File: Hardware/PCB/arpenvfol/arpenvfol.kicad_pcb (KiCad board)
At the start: 2 copper layers, 0 parts

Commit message: Better .gitignore; misc revisions
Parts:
- added C1: 10uF, ao_tht:CP_Radial_D6.3mm_P2.50mm, B.Cu at (96.2, 83.5)
- added C11: 20pF, ao_tht:C_Disc_D3.0mm_W1.6mm_P2.50mm, B.Cu at (83.5, 63.2)
- added C12: 1uF, ao_tht:C_Rect_L7.2mm_W2.5mm_P5.00mm_FKS2_FKP2_MKS2_MKP2, B.Cu at (91.1, 40.3)
- added C13: 100nF, ao_tht:C_Rect_L7.2mm_W2.5mm_P5.00mm_FKS2_FKP2_MKS2_MKP2, B.Cu at (98.7, 50.4)
- added C14: 10uF, ao_tht:C_Radial_D8.0mm_H11.5mm_P3.50mm, B.Cu at (116.5, 108.9)
- added C15: 10nF, ao_tht:C_Rect_L7.2mm_W2.5mm_P5.00mm_FKS2_FKP2_MKS2_MKP2, B.Cu at (106.3, 40.3)
- added C16: 10pF, ao_tht:C_Disc_D3.0mm_W1.6mm_P2.50mm, B.Cu at (108.9, 67.0)
- added C17: 2nF, ao_tht:C_Rect_L7.2mm_W2.5mm_P5.00mm_FKS2_FKP2_MKS2_MKP2, B.Cu at (114.0, 50.4)
- added C18: 47pF, ao_tht:C_Disc_D3.0mm_W1.6mm_P2.50mm, B.Cu at (119.0, 67.0)
- added C19: 1nF, ao_tht:C_Rect_L7.2mm_W2.5mm_P5.00mm_FKS2_FKP2_MKS2_MKP2, B.Cu at (115.3, 61.9)
- added C2: 10uF, ao_tht:CP_Radial_D6.3mm_P2.50mm, B.Cu at (103.8, 83.5)
- added C20: 100nF, ao_tht:C_Disc_D3.0mm_W1.6mm_P2.50mm, B.Cu at (91.1, 63.2)
- added C21: 100nF, ao_tht:C_Disc_D3.0mm_W1.6mm_P2.50mm, B.Cu at (111.4, 61.9)
- added C3: 10uF, ao_tht:C_Radial_D8.0mm_H11.5mm_P3.50mm, B.Cu at (79.7, 108.9)
- added C4: 100uF, ao_tht:CP_Radial_D6.3mm_P2.50mm, B.Cu at (87.3, 116.5)
- added C5: 100nF, ao_tht:C_Rect_L7.2mm_W2.5mm_P5.00mm_FKS2_FKP2_MKS2_MKP2, B.Cu at (106.3, 136.8)
- added C6: 20pF, ao_tht:C_Disc_D3.0mm_W1.6mm_P2.50mm, B.Cu at (88.6, 70.8)
- added C7: 20pF, ao_tht:C_Disc_D3.0mm_W1.6mm_P2.50mm, B.Cu at (81.0, 83.5)
- added C8: 220uF, ao_tht:CP_Radial_D6.3mm_P2.50mm, B.Cu at (87.3, 124.1)
- added C9: 220uF, ao_tht:CP_Radial_D6.3mm_P2.50mm, B.Cu at (91.1, 98.7)
- added D1: 1N5817, ao_tht:D_DO-41_SOD81_P10.16mm_Horizontal, B.Cu at (94.9, 78.4)
- added D2: 1N5817, ao_tht:D_DO-41_SOD81_P10.16mm_Horizontal, B.Cu at (110.2, 94.9)
- added D3: 1N4148, ao_tht:D_DO-35_SOD27_P7.62mm_Horizontal, B.Cu at (96.2, 74.6)
- added D4: 1N4148, ao_tht:D_DO-35_SOD27_P7.62mm_Horizontal, B.Cu at (83.5, 83.5)
- added GRAF1: Holes, arpenvfol:arpenvfol_panel_holes, F.Cu at (100.0, 100.0)
- added J1: Synth_power_2x5, ao_tht:Power_Header, B.Cu at (116.5, 94.9)
- added J10: 3_pin_Molex_header, ao_tht:Molex_KK-254_AE-6410-03A_1x03_P2.54mm_Vertical, B.Cu at (97.5, 135.6)
- added J2: AudioJack2_SwitchT, ao_tht:Jack_6.35mm_PJ_629HAN_slots, F.Cu at (87.5, 150.0)
- added J3: AudioJack2_SwitchT, ao_tht:Jack_6.35mm_PJ_629HAN_slots, F.Cu at (112.5, 125.0)
- added J4: AudioJack2_SwitchT, ao_tht:Jack_6.35mm_PJ_629HAN_slots, F.Cu at (112.5, 150.0)
- added J5: AudioJack2, ao_tht:Jack_6.35mm_PJ_629HAN_slots, F.Cu at (112.5, 175.0)
- added J6: AudioJack2, ao_tht:Jack_6.35mm_PJ_629HAN_slots, F.Cu at (87.5, 175.0)
- added J8: 2_pin_Molex_header, ao_tht:Molex_KK-254_AE-6410-02A_1x02_P2.54mm_Vertical, B.Cu at (84.8, 135.6)
- added Q1: 2N3904, ao_tht:TO-92_Inline_Wide, B.Cu at (88.6, 111.4)
- added Q2: 2N3904, ao_tht:TO-92_Inline_Wide, B.Cu at (94.9, 111.4)
- added R1: 1k, ao_tht:R_Axial_DIN0207_L6.3mm_D2.5mm_P10.16mm_Horizontal, B.Cu at (79.7, 91.1)
- added R10: 1k, ao_tht:R_Axial_DIN0207_L6.3mm_D2.5mm_P10.16mm_Horizontal, B.Cu at (96.2, 91.1)
- added R11: 1k, ao_tht:R_Axial_DIN0207_L6.3mm_D2.5mm_P10.16mm_Horizontal, B.Cu at (100.0, 116.5)
- added R12: 100k, ao_tht:R_Axial_DIN0207_L6.3mm_D2.5mm_P10.16mm_Horizontal, B.Cu at (83.5, 40.3)
- added R13: 120k, ao_tht:R_Axial_DIN0207_L6.3mm_D2.5mm_P10.16mm_Horizontal, B.Cu at (91.1, 59.4)
- added R14: 100k, ao_tht:R_Axial_DIN0207_L6.3mm_D2.5mm_P10.16mm_Horizontal, B.Cu at (81.0, 55.5)
- added R15: 2.7k, ao_tht:R_Axial_DIN0207_L6.3mm_D2.5mm_P10.16mm_Horizontal, B.Cu at (87.3, 50.5)
- added R16: 27k, ao_tht:R_Axial_DIN0207_L6.3mm_D2.5mm_P10.16mm_Horizontal, B.Cu at (94.9, 40.3)
- added R17: 1M, ao_tht:R_Axial_DIN0207_L6.3mm_D2.5mm_P10.16mm_Horizontal, B.Cu at (109.0, 111.4)
- added R18: 270k, ao_tht:R_Axial_DIN0207_L6.3mm_D2.5mm_P10.16mm_Horizontal, B.Cu at (102.5, 50.5)
- added R19: 150k, ao_tht:R_Axial_DIN0207_L6.3mm_D2.5mm_P10.16mm_Horizontal, B.Cu at (105.1, 101.3)
- added R2: 82k, ao_tht:R_Axial_DIN0207_L6.3mm_D2.5mm_P10.16mm_Horizontal, B.Cu at (120.3, 136.8)
- added R20: 1M, ao_tht:R_Axial_DIN0207_L6.3mm_D2.5mm_P10.16mm_Horizontal, B.Cu at (110.2, 40.3)
- added R21: 1k, ao_tht:R_Axial_DIN0207_L6.3mm_D2.5mm_P10.16mm_Horizontal, B.Cu at (108.9, 74.6)
- added R22: 1.5M, ao_tht:R_Axial_DIN0207_L6.3mm_D2.5mm_P10.16mm_Horizontal, B.Cu at (119.0, 58.1)
- added R23: 10k, ao_tht:R_Axial_DIN0207_L6.3mm_D2.5mm_P10.16mm_Horizontal, B.Cu at (119.0, 70.8)
- added R24: 10M, ao_tht:R_Axial_DIN0207_L6.3mm_D2.5mm_P10.16mm_Horizontal, B.Cu at (119.0, 54.3)
- added R25: 100k, ao_tht:R_Axial_DIN0207_L6.3mm_D2.5mm_P10.16mm_Horizontal, B.Cu at (101.3, 101.3)
- added R26: 100k, ao_tht:R_Axial_DIN0207_L6.3mm_D2.5mm_P10.16mm_Horizontal, B.Cu at (106.3, 162.2)
- added R27: 1k, ao_tht:R_Axial_DIN0207_L6.3mm_D2.5mm_P10.16mm_Horizontal, B.Cu at (110.2, 162.2)
- added R28: 1k, ao_tht:R_Axial_DIN0207_L6.3mm_D2.5mm_P10.16mm_Horizontal, B.Cu at (92.4, 162.2)
- added R3: 22k, ao_tht:R_Axial_DIN0207_L6.3mm_D2.5mm_P10.16mm_Horizontal, B.Cu at (84.8, 91.1)
- added R4: 10k, ao_tht:R_Axial_DIN0207_L6.3mm_D2.5mm_P10.16mm_Horizontal, B.Cu at (94.9, 116.5)
- added R5: 39k, ao_tht:R_Axial_DIN0207_L6.3mm_D2.5mm_P10.16mm_Horizontal, B.Cu at (91.1, 67.0)
- added R6: 100k, ao_tht:R_Axial_DIN0207_L6.3mm_D2.5mm_P10.16mm_Horizontal, B.Cu at (91.1, 79.7)
- added R7: 100k, ao_tht:R_Axial_DIN0207_L6.3mm_D2.5mm_P10.16mm_Horizontal, B.Cu at (80.9, 74.6)
- added R8: 10k, ao_tht:R_Axial_DIN0207_L6.3mm_D2.5mm_P10.16mm_Horizontal, B.Cu at (81.0, 116.5)
- added R9: 100k, ao_tht:R_Axial_DIN0207_L6.3mm_D2.5mm_P10.16mm_Horizontal, B.Cu at (91.1, 87.3)
- added TP1: -12V, ao_tht:TestPoint_THTPad_D1.5mm_Drill0.7mm, B.Cu at (121.6, 50.5)
- added TP2: +12V, ao_tht:TestPoint_THTPad_D1.5mm_Drill0.7mm, B.Cu at (121.6, 40.3)
- added TP3: GND, ao_tht:TestPoint_THTPad_1.5x1.5mm_Drill0.7mm, B.Cu at (121.6, 45.4)
- added U1: TL074, ao_tht:DIP-14_W7.62mm_Socket_LongPads, B.Cu at (103.8, 55.5)
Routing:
- net Net-(C19-Pad2): track 0.00 -> 137.8 mm
- net PREAMP_OUT: track 0.00 -> 120.1 mm
- net +12V: track 0.00 -> 103.6 mm
- net /Main PCB/SIGNAL_ATT: track 0.00 -> 77.1 mm
- net Net-(J4-PadTN): track 0.00 -> 62.4 mm
- net Net-(C14-Pad2): track 0.00 -> 54.6 mm
- net -12V: track 0.00 -> 54.2 mm
- net Net-(D3-Pad2): track 0.00 -> 49.0 mm
- net /Main PCB/MIC_IN: track 0.00 -> 45.4 mm
- net /Main PCB/INST_IN: track 0.00 -> 42.1 mm
- net Net-(C8-Pad1): track 0.00 -> 40.1 mm
- net Net-(C11-Pad1): track 0.00 -> 35.3 mm
- net Net-(C7-Pad1): track 0.00 -> 31.4 mm
- net Net-(C11-Pad2): track 0.00 -> 28.0 mm
- net Net-(C18-Pad1): track 0.00 -> 24.3 mm
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- added copper zone on B.Cu, net GND
- added copper zone on F.Cu, net GND
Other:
- board outline added: 46 x 147 mm

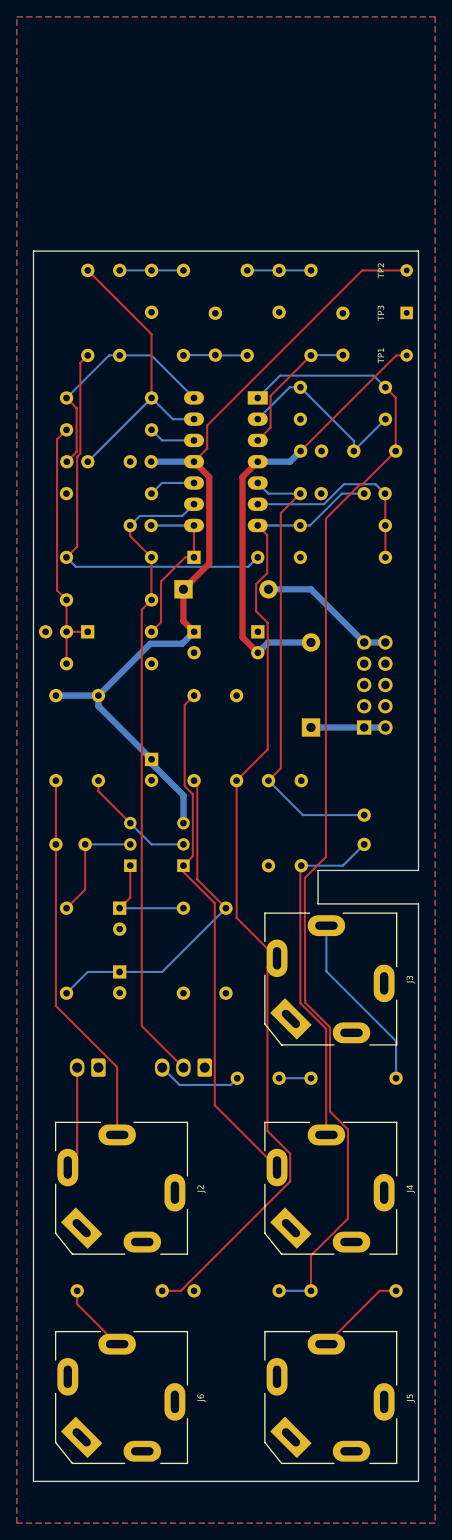
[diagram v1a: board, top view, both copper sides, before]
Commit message: Reorganize schem; add resistor to mic preamp; change EF gain; add simulation
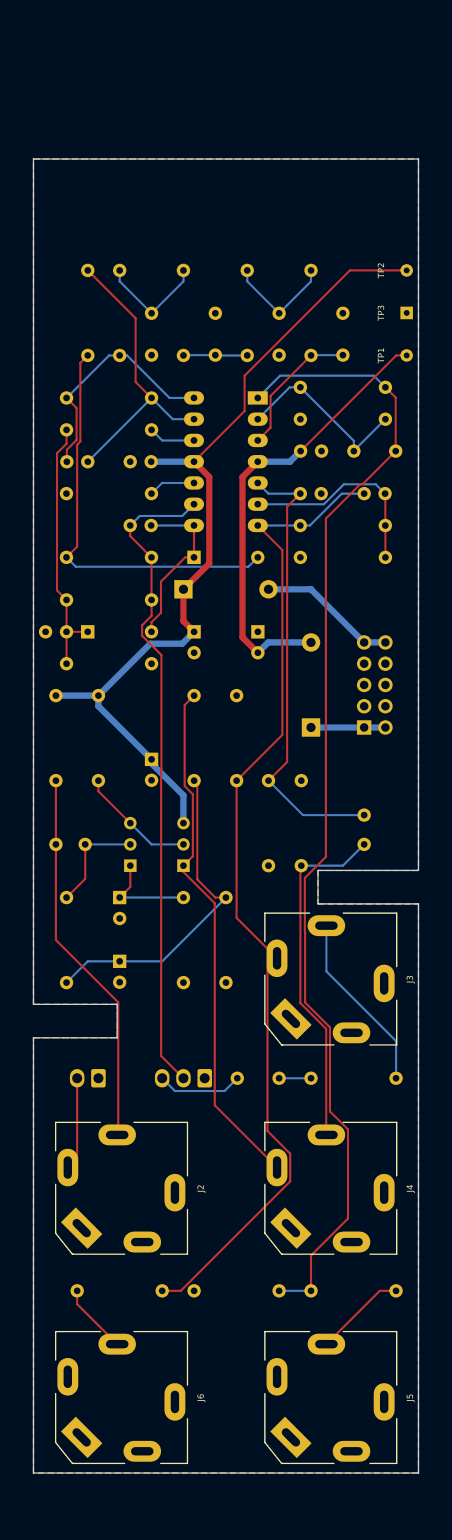
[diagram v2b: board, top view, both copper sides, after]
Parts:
- added GRAF2: AO logo, ao_tht:analogoutput_12mm, B.Cu at (114.5, 34.3)
- added GRAF3: CC0 logo, ao_tht:CC0_logo, B.Cu at (79.0, 45.0)
- moved C12 5.12 mm to (91.1, 45.4)
- moved C15 5.12 mm to (106.3, 45.4)
- moved C4 1.27 mm to (87.3, 115.2)
- moved J10 1.27 mm to (97.5, 136.8)
- moved J8 1.27 mm to (84.8, 136.8)
- moved R11 1.27 mm to (100.0, 115.2)
- moved R4 1.27 mm to (94.9, 115.2)
- moved R8 1.27 mm to (81.0, 115.2)
- moved C8 1.27 mm to (87.3, 122.9)
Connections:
- net /Main PCB/EF_OUT renamed /EF_OUT
- net /Main PCB/INST_IN renamed /INST_IN
- net /Main PCB/MIC renamed MIC
- net /Main PCB/MIC_IN renamed /MIC_IN
- net /Main PCB/PRE_OUT renamed /PRE_OUT
- net /Main PCB/SIGNAL_AC renamed SIGNAL_AC
- net /Main PCB/SIGNAL_ATT renamed SIGNAL_ATT
- net /Main PCB/SIGNAL_IN renamed /SIGNAL_IN
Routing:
- net Net-(C15-Pad1): track 7.62 -> 13.4 mm
- net Net-(C12-Pad1): track 7.62 -> 13.4 mm
- net MIC: track 12.4 -> 11.1 mm
- net Net-(C4-Pad1): track 13.2 -> 12.0 mm
- net Net-(C3-Pad2): track 13.9 -> 12.7 mm
- net SIGNAL_ATT: track 77.1 -> 78.3 mm
- net +12V: track 103.6 -> 104.5 mm
- net Net-(C8-Pad1): track 40.1 -> 39.6 mm
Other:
- board size 46 x 147 mm -> 46 x 157 mm
- board text added: "Envelope Follower"
- board text added: "Rich Holmes / Feb 2022 / CC0 1.0"
- board text added: "https://github.com/holmesrichards/arpenvfol"

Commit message: Change transistor, annotate, LTSpice simulation
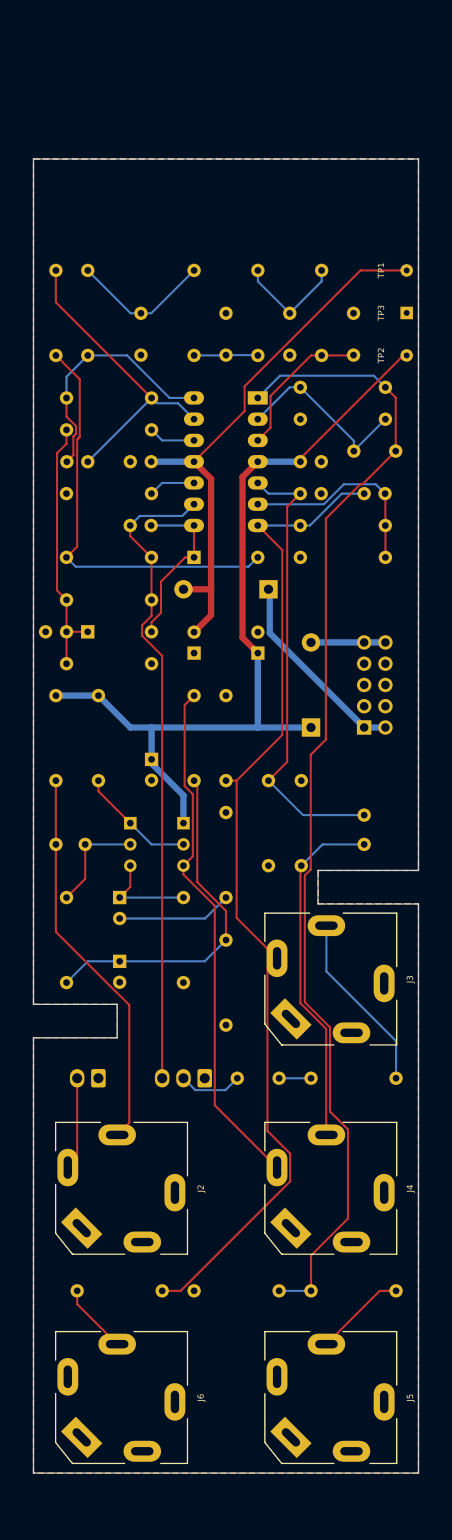
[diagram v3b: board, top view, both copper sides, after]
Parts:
- added R29: 1k, ao_tht:R_Axial_DIN0207_L6.3mm_D2.5mm_P10.16mm_Horizontal, B.Cu at (100.0, 115.2)
- C12: footprint ao_tht:C_Rect_L7.2mm_W2.5mm_P5.00mm_FKS2_FKP2_MKS2_MKP2 -> ao_tht:C_Rect_L7.2mm_W7.2mm_P5.00mm_FKS2_FKP2_MKS2_MKP2
- Q1, Q2: value 2N3904 -> BC549
- R24: value 10M -> 3M
- moved GRAF3 130.6 mm to (100.1, 173.9)
- moved C21 22.9 mm to (88.6, 63.2), turned to 0 degrees
- moved D1 22.5 mm to (110.2, 94.9), turned to 90 degrees
- moved C20 17.8 mm to (108.9, 63.2), turned to 0 degrees
- moved D2 17.3 mm to (105.1, 78.4), turned to 180 degrees
- moved TP1 10.2 mm to (121.6, 40.3)
- moved TP2 10.2 mm to (121.6, 50.5)
- moved C1 8.03 mm to (103.8, 86.0), turned to 90 degrees
- moved C2 8.03 mm to (96.2, 86.0), turned to 90 degrees
- moved Q1 5.08 mm to (88.6, 106.3), turned to -90 degrees
- moved Q2 5.08 mm to (94.9, 106.3), turned to -90 degrees
- moved R11 5.08 mm to (100.0, 120.3)
- moved R15 3.81 mm to (83.5, 50.5)
- moved R12 3.81 mm to (79.7, 40.3)
- moved C15 1.27 mm to (107.6, 45.4)
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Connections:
- C4 pad 2: GND -> Net-(C4-Pad2)
- J10 pad 2: SIGNAL_ATT -> SIGNAL_AC
- J10 pad 3: SIGNAL_AC -> SIGNAL_ATT
- Q1 pad 1: Net-(C4-Pad1) -> Net-(Q1-Pad1)
- Q1 pad 3: Net-(Q1-Pad3) -> Net-(C4-Pad1)
- Q2 pad 1: Net-(J4-PadTN) -> +12V
- Q2 pad 2: Net-(Q1-Pad3) -> Net-(Q1-Pad1)
- Q2 pad 3: +12V -> Net-(J4-PadTN)
- R3 pad 2: Net-(Q1-Pad3) -> Net-(Q1-Pad1)
- U1 pad 11: +12V -> -12V
- U1 pad 4: -12V -> +12V
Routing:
- net /-12_IN: track 8.89 -> 23.8 mm
- net Net-(Q1-Pad3): track 14.1 -> 0.00 mm
- net Net-(Q1-Pad1): track 0.00 -> 14.1 mm
- net Net-(C4-Pad2): track 0.00 -> 13.7 mm
- net -12V: track 54.2 -> 67.1 mm
- net /+12_IN: track 16.6 -> 8.89 mm
- net Net-(C12-Pad1): track 13.4 -> 16.9 mm
- net +12V: track 104.5 -> 101.6 mm
- net SIGNAL_AC: track 10.2 -> 7.61 mm
- net Net-(C8-Pad1): track 39.6 -> 41.8 mm
- net Net-(C11-Pad1): track 35.3 -> 36.9 mm
- net Net-(C11-Pad2): track 28.0 -> 29.5 mm
- net Net-(C17-Pad1): track 16.6 -> 17.9 mm
- net PREAMP_OUT: track 120.4 -> 121.7 mm
- net /MIC_IN: track 45.5 -> 46.6 mm
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
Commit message: Panel; add gain pot
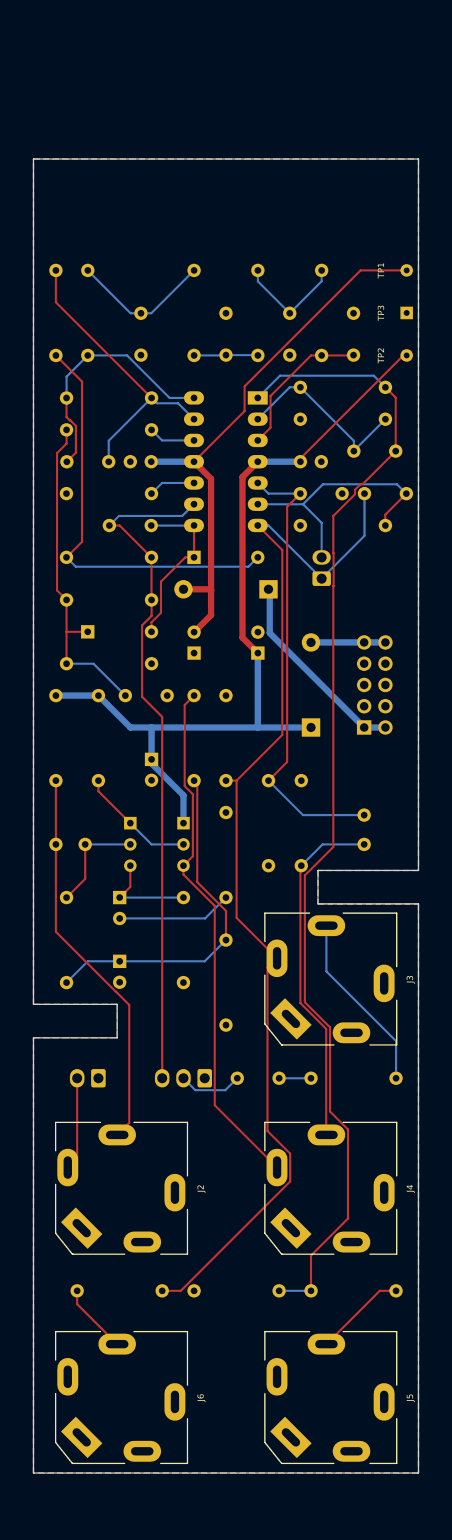
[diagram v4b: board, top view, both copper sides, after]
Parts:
- removed R23: 10k, ao_tht:R_Axial_DIN0207_L6.3mm_D2.5mm_P10.16mm_Horizontal
- added J12: 2_pin_Molex_header, ao_tht:Molex_KK-254_AE-6410-02A_1x02_P2.54mm_Vertical, B.Cu at (111.4, 77.1)
- C11, C16, C18, C6, C7: footprint ao_tht:C_Disc_D3.0mm_W1.6mm_P2.50mm -> ao_tht:C_Disc_D5.0mm_W2.5mm_P5.00mm
- moved C7 10.4 mm to (88.0, 91.1), turned to 0 degrees
- moved R21 3.81 mm to (108.9, 70.8)
- moved C18 2.54 mm to (121.5, 67.0)
- moved C11 2.50 mm to (86.0, 63.2)
- moved C6 2.49 mm to (86.1, 70.8)
- moved GRAF2 1.35 mm to (115.5, 33.5)
- turned GRAF3 to 180 degrees
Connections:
- net Net-(C18-Pad1) renamed GAIN_W
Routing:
- net Net-(C7-Pad1): track 31.4 -> 40.0 mm
- net PREAMP_OUT: track 121.7 -> 130.0 mm
- net GAIN_W: track 24.3 -> 31.3 mm
- net SIGNAL_ATT: track 77.2 -> 81.5 mm
- net Net-(C11-Pad1): track 36.9 -> 35.8 mm
- net +12V: track 101.6 -> 100.8 mm
- net Net-(C8-Pad1): track 41.8 -> 41.2 mm
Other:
- board text added: "EF OUT"
- board text added: "GAIN W / CCW"
- board text added: "GND / MIC"
- board text added: "GND / SIG W / SIG CW"
- board text added: "INST IN"
- board text added: "MIC IN"
- board text added: "PRE OUT"
- board text added: "Rich Holmes / Mar 2022 / CC0 1.0 based on ARP and Ken Stone designs"
- board text added: "SIG IN"
- board text removed: "Rich Holmes / Feb 2022 / CC0 1.0"

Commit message: Final pre fab tweaks, Gerbers, schematic, BOM
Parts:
- renumbered C4 to C1, C20 to C10, C21 to C11, C11 to C12, C12 to C13, C13 to C14, C14 to C15, C15 to C16, C16 to C17, C17 to C18, C18 to C19, C5 to C2, C19 to C20, C6 to C4, C7 to C5, C1 to C6, C2 to C7, J2 to J1, J5 to J11, J6 to J12, J3 to J2, J1 to J3, J12 to J9, R8 to R10, R10 to R11, R11 to R12, R12 to R13, R13 to R14, R14 to R15, R15 to R16, R16 to R17, R17 to R18, R18 to R19, R19 to R20, R20 to R21, R21 to R23, R26 to R25, R25 to R26, R29 to R3, R5 to R4, R3 to R5, R4 to R6, R6 to R7, R7 to R8
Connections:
- net Net-(J4-PadTN) renamed MIC_OUT
- net PREAMP_OUT renamed GAIN_CCW

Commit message: Update PCB, layout files
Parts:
- C18: value 2nF -> 2.2nF
- R23: value 1k -> 470R
- R24: value 3M -> 4.7M
